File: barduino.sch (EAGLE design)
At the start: 28 parts, among them Q2 16MHz

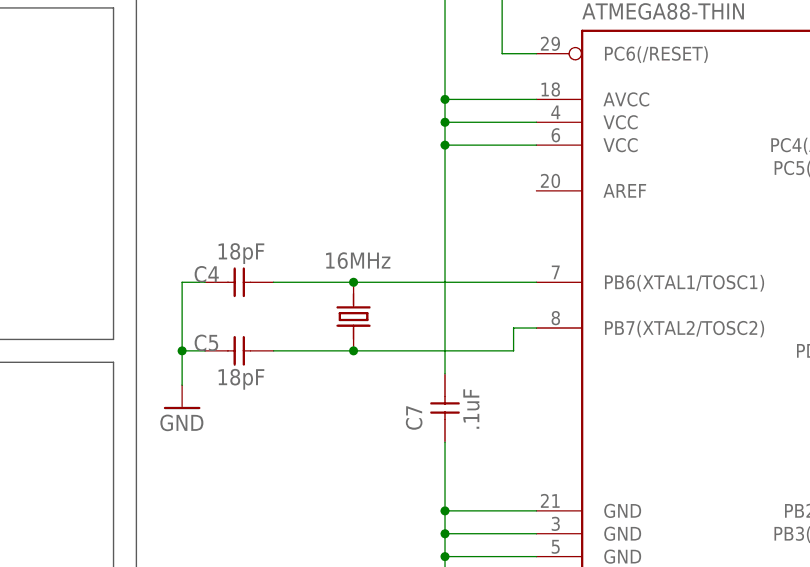
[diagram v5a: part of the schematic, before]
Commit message: replace crystal with new footprint part
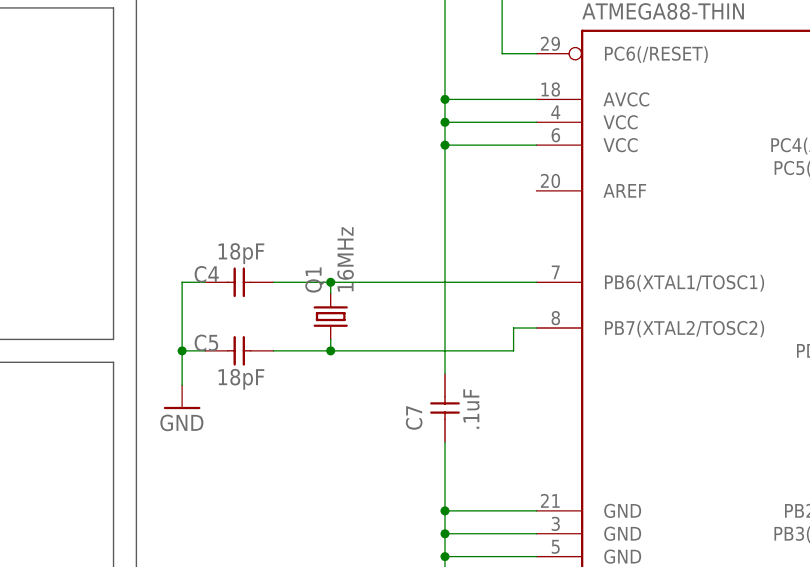
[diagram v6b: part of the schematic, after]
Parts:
- removed Q2: 16MHz, ng:CRYSTALCS10
- added Q1: 16MHz, crystal:CRYSTALHC49UP
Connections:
- net PB6: now also Q1.2; no longer Q2.2
- net PB7: now also Q1.1; no longer Q2.1
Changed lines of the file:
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@@
 <part name="P+3" library="supply1" deviceset="VCC" device=""/>
 <part name="GND4" library="supply1" deviceset="GND" device=""/>
-<part name="Q2" library="ng" deviceset="CRYSTAL" device="CS10" value="16MHz"/>
 <part name="C4" library="ng" deviceset="UNPOLARIZED_CAPACITOR" device="1206" value="18pF"/>
 <part name="C5" library="ng" deviceset="UNPOLARIZED_CAPACITOR" device="1206" value="18pF"/>
@@
 <part name="U$5" library="4-Digit-Clock" deviceset="MICRO-USB-PWR" device=""/>
 <part name="R13" library="resistor" library_urn="urn:adsk.eagle:library:348" deviceset="R-US_" device="R1206" package3d_urn="urn:adsk.eagle:package:26062/1"/>
+<part name="Q1" library="crystal" library_urn="urn:adsk.eagle:library:204" deviceset="CRYSTAL" device="HC49UP" package3d_urn="urn:adsk.eagle:package:12078/1" value="16MHz"/>
 </parts>
 <sheets>
@@
 <instance part="P+3" gate="VCC" x="213.36" y="110.49"/>
 <instance part="GND4" gate="1" x="184.15" y="45.72"/>
-<instance part="Q2" gate="G$1" x="203.2" y="55.88" smashed="yes" rot="R90">
-<attribute name="VALUE" x="199.898" y="61.214" size="1.778" layer="96"/>
-</instance>
 <instance part="C4" gate="1" x="191.77" y="59.69" smashed="yes">
 <attribute name="NAME" x="185.42" y="59.69" size="1.778" layer="95"/>
@@
 <instance part="U$5" gate="G$1" x="15.24" y="92.71" rot="MR0"/>
 <instance part="R13" gate="G$1" x="26.67" y="97.79" rot="R180"/>
+<instance part="Q1" gate="G$1" x="200.66" y="55.88" rot="R90"/>
 </instances>
 <busses>
@@
 <net name="PB7" class="0">
 <segment>
-<wire x1="203.2" y1="52.07" x2="194.31" y2="52.07" width="0.1524" layer="91"/>
-<pinref part="Q2" gate="G$1" pin="1"/>
 <pinref part="C5" gate="1" pin="2"/>
 <pinref part="U$1" gate="G$1" pin="PB7(XTAL2/TOSC2)"/>
 <wire x1="223.52" y1="54.61" x2="220.98" y2="54.61" width="0.1524" layer="91"/>
 <wire x1="220.98" y1="54.61" x2="220.98" y2="52.07" width="0.1524" layer="91"/>
-<wire x1="220.98" y1="52.07" x2="203.2" y2="52.07" width="0.1524" layer="91"/>
-<junction x="203.2" y="52.07"/>
+<wire x1="220.98" y1="52.07" x2="200.66" y2="52.07" width="0.1524" layer="91"/>
+<pinref part="Q1" gate="G$1" pin="1"/>
+<wire x1="200.66" y1="52.07" x2="194.31" y2="52.07" width="0.1524" layer="91"/>
+<wire x1="200.66" y1="53.34" x2="200.66" y2="52.07" width="0.1524" layer="91"/>
+<junction x="200.66" y="52.07"/>
 </segment>
 </net>
@@
 <net name="PB6" class="0">
 <segment>
-<wire x1="194.31" y1="59.69" x2="203.2" y2="59.69" width="0.1524" layer="91"/>
-<pinref part="Q2" gate="G$1" pin="2"/>
 <pinref part="C4" gate="1" pin="2"/>
 <pinref part="U$1" gate="G$1" pin="PB6(XTAL1/TOSC1)"/>
-<wire x1="223.52" y1="59.69" x2="203.2" y2="59.69" width="0.1524" layer="91"/>
-<junction x="203.2" y="59.69"/>
-</segment>
-</net>
+<wire x1="223.52" y1="59.69" x2="200.66" y2="59.69" width="0.1524" layer="91"/>
+<pinref part="Q1" gate="G$1" pin="2"/>
+<wire x1="200.66" y1="59.69" x2="194.31" y2="59.69" width="0.1524" layer="91"/>
+<wire x1="200.66" y1="58.42" x2="200.66" y2="59.69" width="0.1524" layer="91"/>
+<junction x="200.66" y="59.69"/>
+</segment>
+</net>

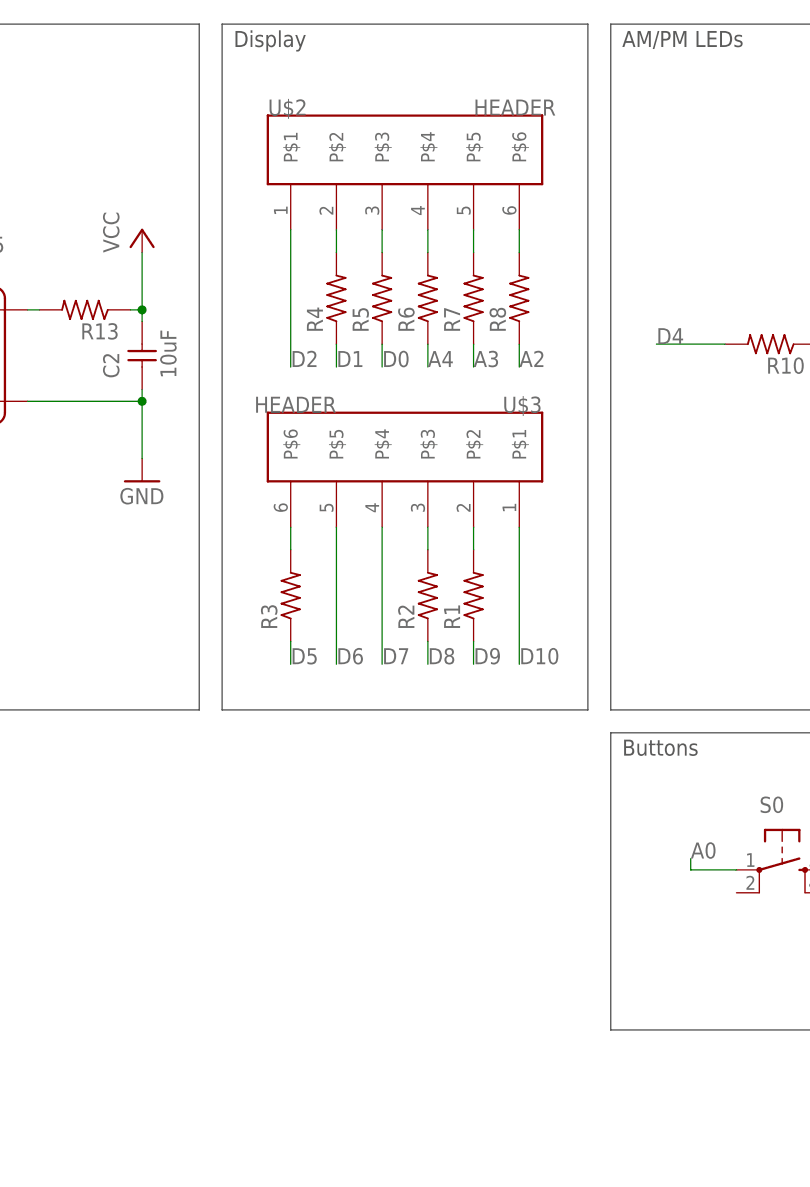
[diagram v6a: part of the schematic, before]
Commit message: add pull ups on display resistors
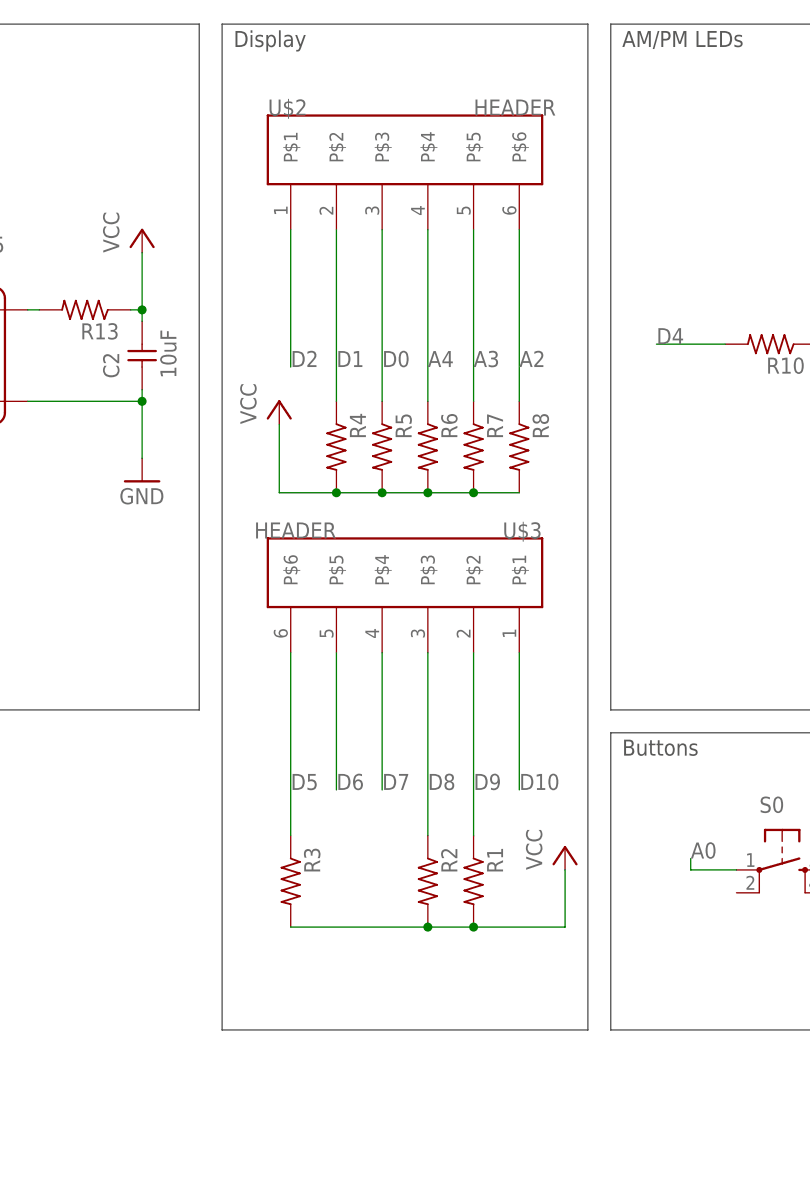
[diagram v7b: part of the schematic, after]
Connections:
- removed net N$10: R5.2, U$2.P$3
- removed net N$22: R4.2, U$2.P$2
- removed net N$23: R6.2, U$2.P$4
- removed net N$29: R2.2, U$3.P$3
- removed net N$33: R1.2, U$3.P$2
- removed net N$4: R3.2, U$3.P$6
- removed net N$8: R8.2, U$2.P$6
- removed net N$9: R7.2, U$2.P$5
- net A2: now also U$2.P$6
- net A3: now also U$2.P$5
- net A4: now also U$2.P$4
- net D0: now also U$2.P$3
- net D1: now also U$2.P$2
- net D5: now also U$3.P$6
- net D8: now also U$3.P$3
- net D9: now also U$3.P$2
- net VCC: now also R1.2, R2.2, R3.2, R4.2, R5.2, R6.2, R7.2, R8.2
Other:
- moved on the sheet: R1, R2, R3, R4, R5, R6, R7, R8, U$3

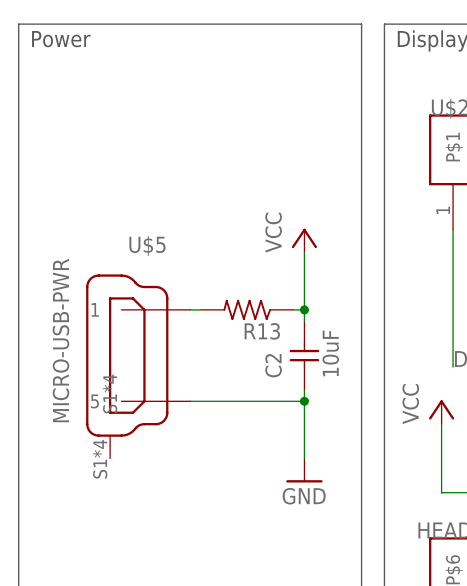
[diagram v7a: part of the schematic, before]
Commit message: change to new USB and buzzer footprint on schematic and layout
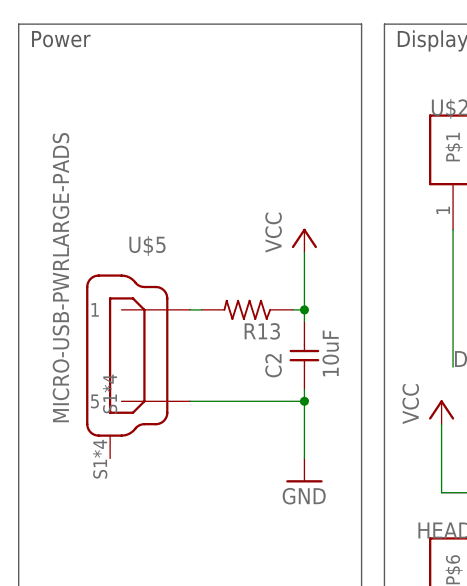
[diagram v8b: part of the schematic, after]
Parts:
- U$4: value BUZZER -> BUZZERLARGE-PADS; device 4-Digit-Clock:BUZZER -> 4-Digit-Clock:BUZZERLARGE-PADS
- U$5: value MICRO-USB-PWR -> MICRO-USB-PWRLARGE-PADS; device 4-Digit-Clock:MICRO-USB-PWR -> 4-Digit-Clock:MICRO-USB-PWRLARGE-PADS
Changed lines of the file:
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@@
 <grid distance="0.05" unitdist="inch" unit="inch" style="lines" multiple="1" display="no" altdistance="0.01" altunitdist="inch" altunit="inch"/>
 <layers>
-<layer number="1" name="Top" color="4" fill="1" visible="no" active="no"/>
-<layer number="2" name="Route2" color="1" fill="3" visible="no" active="no"/>
-<layer number="3" name="Route3" color="4" fill="3" visible="no" active="no"/>
-<layer number="4" name="Route4" color="1" fill="4" visible="no" active="no"/>
-<layer number="5" name="Route5" color="4" fill="4" visible="no" active="no"/>
-<layer number="6" name="Route6" color="1" fill="8" visible="no" active="no"/>
-<layer number="7" name="Route7" color="4" fill="8" visible="no" active="no"/>
-<layer number="8" name="Route8" color="1" fill="2" visible="no" active="no"/>
-<layer number="9" name="Route9" color="4" fill="2" visible="no" active="no"/>
-<layer number="10" name="Route10" color="1" fill="7" visible="no" active="no"/>
-<layer number="11" name="Route11" color="4" fill="7" visible="no" active="no"/>
-<layer number="12" name="Route12" color="1" fill="5" visible="no" active="no"/>
-<layer number="13" name="Route13" color="4" fill="5" visible="no" active="no"/>
-<layer number="14" name="Route14" color="1" fill="6" visible="no" active="no"/>
-<layer number="15" name="Route15" color="4" fill="6" visible="no" active="no"/>
-<layer number="16" name="Bottom" color="1" fill="1" visible="no" active="no"/>
-<layer number="17" name="Pads" color="2" fill="1" visible="no" active="no"/>
-<layer number="18" name="Vias" color="2" fill="1" visible="no" active="no"/>
-<layer number="19" name="Unrouted" color="6" fill="1" visible="no" active="no"/>
-<layer number="20" name="Dimension" color="15" fill="1" visible="no" active="no"/>
-<layer number="21" name="tPlace" color="7" fill="1" visible="no" active="no"/>
-<layer number="22" name="bPlace" color="7" fill="1" visible="no" active="no"/>
-<layer number="23" name="tOrigins" color="15" fill="1" visible="no" active="no"/>
-<layer number="24" name="bOrigins" color="15" fill="1" visible="no" active="no"/>
-<layer number="25" name="tNames" color="7" fill="1" visible="no" active="no"/>
-<layer number="26" name="bNames" color="7" fill="1" visible="no" active="no"/>
-<layer number="27" name="tValues" color="7" fill="1" visible="no" active="no"/>
-<layer number="28" name="bValues" color="7" fill="1" visible="no" active="no"/>
+<layer number="1" name="Top" color="12" fill="1" visible="yes" active="no"/>
+<layer number="2" name="Route2" color="1" fill="3" visible="yes" active="no"/>
+<layer number="3" name="Route3" color="4" fill="3" visible="yes" active="no"/>
+<layer number="4" name="Route4" color="1" fill="4" visible="yes" active="no"/>
+<layer number="5" name="Route5" color="4" fill="4" visible="yes" active="no"/>
+<layer number="6" name="Route6" color="1" fill="8" visible="yes" active="no"/>
+<layer number="7" name="Route7" color="4" fill="8" visible="yes" active="no"/>
+<layer number="8" name="Route8" color="1" fill="2" visible="yes" active="no"/>
+<layer number="9" name="Route9" color="4" fill="2" visible="yes" active="no"/>
+<layer number="10" name="Route10" color="1" fill="7" visible="yes" active="no"/>
+<layer number="11" name="Route11" color="4" fill="7" visible="yes" active="no"/>
+<layer number="12" name="Route12" color="1" fill="5" visible="yes" active="no"/>
+<layer number="13" name="Route13" color="4" fill="5" visible="yes" active="no"/>
+<layer number="14" name="Route14" color="1" fill="6" visible="yes" active="no"/>
+<layer number="15" name="Route15" color="4" fill="6" visible="yes" active="no"/>
+<layer number="16" name="Bottom" color="1" fill="1" visible="yes" active="no"/>
+<layer number="17" name="Pads" color="2" fill="1" visible="yes" active="no"/>
+<layer number="18" name="Vias" color="2" fill="1" visible="yes" active="no"/>
+<layer number="19" name="Unrouted" color="6" fill="1" visible="yes" active="no"/>
+<layer number="20" name="Dimension" color="15" fill="1" visible="yes" active="no"/>
+<layer number="21" name="tPlace" color="7" fill="1" visible="yes" active="no"/>
+<layer number="22" name="bPlace" color="7" fill="1" visible="yes" active="no"/>
+<layer number="23" name="tOrigins" color="15" fill="1" visible="yes" active="no"/>
+<layer number="24" name="bOrigins" color="15" fill="1" visible="yes" active="no"/>
+<layer number="25" name="tNames" color="7" fill="1" visible="yes" active="no"/>
+<layer number="26" name="bNames" color="7" fill="1" visible="yes" active="no"/>
+<layer number="27" name="tValues" color="7" fill="1" visible="yes" active="no"/>
+<layer number="28" name="bValues" color="7" fill="1" visible="yes" active="no"/>
 <layer number="29" name="tStop" color="7" fill="3" visible="no" active="no"/>
 <layer number="30" name="bStop" color="7" fill="6" visible="no" active="no"/>
@@
 <layer number="35" name="tGlue" color="7" fill="4" visible="no" active="no"/>
 <layer number="36" name="bGlue" color="7" fill="5" visible="no" active="no"/>
-<layer number="37" name="tTest" color="7" fill="1" visible="no" active="no"/>
-<layer number="38" name="bTest" color="7" fill="1" visible="no" active="no"/>
+<layer number="37" name="tTest" color="7" fill="1" visible="yes" active="no"/>
+<layer number="38" name="bTest" color="7" fill="1" visible="yes" active="no"/>
 <layer number="39" name="tKeepout" color="4" fill="11" visible="no" active="no"/>
 <layer number="40" name="bKeepout" color="1" fill="11" visible="no" active="no"/>
@@
 <layer number="44" name="Drills" color="7" fill="1" visible="no" active="no"/>
 <layer number="45" name="Holes" color="7" fill="1" visible="no" active="no"/>
-<layer number="46" name="Milling" color="3" fill="1" visible="no" active="no"/>
-<layer number="47" name="Measures" color="7" fill="1" visible="no" active="no"/>
-<layer number="48" name="Document" color="7" fill="1" visible="no" active="no"/>
-<layer number="49" name="Reference" color="7" fill="1" visible="no" active="no"/>
-<layer number="50" name="dxf" color="7" fill="1" visible="no" active="no"/>
-<layer number="51" name="tDocu" color="7" fill="1" visible="no" active="no"/>
-<layer number="52" name="bDocu" color="7" fill="1" visible="no" active="no"/>
-<layer number="53" name="tGND_GNDA" color="7" fill="9" visible="no" active="no"/>
-<layer number="54" name="bGND_GNDA" color="1" fill="9" visible="no" active="no"/>
-<layer number="56" name="wert" color="7" fill="1" visible="no" active="no"/>
-<layer number="57" name="tCAD" color="7" fill="1" visible="no" active="no"/>
-<layer number="59" name="tCarbon" color="7" fill="1" visible="no" active="no"/>
-<layer number="60" name="bCarbon" color="7" fill="1" visible="no" active="no"/>
+<layer number="46" name="Milling" color="3" fill="1" visible="yes" active="no"/>
+<layer number="47" name="Measures" color="7" fill="1" visible="yes" active="no"/>
+<layer number="48" name="Document" color="7" fill="1" visible="yes" active="no"/>
+<layer number="49" name="Reference" color="7" fill="1" visible="yes" active="no"/>
+<layer number="50" name="dxf" color="7" fill="1" visible="yes" active="no"/>
+<layer number="51" name="tDocu" color="7" fill="1" visible="yes" active="no"/>
+<layer number="52" name="bDocu" color="7" fill="1" visible="yes" active="no"/>
+<layer number="53" name="tGND_GNDA" color="7" fill="9" visible="yes" active="no"/>
+<layer number="54" name="bGND_GNDA" color="1" fill="9" visible="yes" active="no"/>
+<layer number="56" name="wert" color="7" fill="1" visible="yes" active="no"/>
+<layer number="57" name="tCAD" color="7" fill="1" visible="yes" active="no"/>
+<layer number="59" name="tCarbon" color="7" fill="1" visible="yes" active="no"/>
+<layer number="60" name="bCarbon" color="7" fill="1" visible="yes" active="no"/>
 <layer number="90" name="Modules" color="5" fill="1" visible="yes" active="yes"/>
 <layer number="91" name="Nets" color="2" fill="1" visible="yes" active="yes"/>
@@
 <part name="GND7" library="supply1" library_urn="urn:adsk.eagle:library:371" deviceset="GND" device=""/>
 <part name="GND3" library="supply1" library_urn="urn:adsk.eagle:library:371" deviceset="GND" device=""/>
-<part name="U$4" library="4-Digit-Clock" deviceset="BUZZER" device=""/>
+<part name="U$4" library="4-Digit-Clock" deviceset="BUZZER" device="LARGE-PADS" value="BUZZERLARGE-PADS"/>
 <part name="R1" library="resistor" library_urn="urn:adsk.eagle:library:348" deviceset="R-US_" device="R1206" package3d_urn="urn:adsk.eagle:package:26062/1"/>
 <part name="R2" library="resistor" library_urn="urn:adsk.eagle:library:348" deviceset="R-US_" device="R1206" package3d_urn="urn:adsk.eagle:package:26062/1"/>
@@
 <part name="R11" library="resistor" library_urn="urn:adsk.eagle:library:348" deviceset="R-US_" device="R1206" package3d_urn="urn:adsk.eagle:package:26062/1"/>
 <part name="R10" library="resistor" library_urn="urn:adsk.eagle:library:348" deviceset="R-US_" device="R1206" package3d_urn="urn:adsk.eagle:package:26062/1"/>
-<part name="U$5" library="4-Digit-Clock" deviceset="MICRO-USB-PWR" device=""/>
+<part name="U$5" library="4-Digit-Clock" deviceset="MICRO-USB-PWR" device="LARGE-PADS" value="MICRO-USB-PWRLARGE-PADS"/>
 <part name="R13" library="resistor" library_urn="urn:adsk.eagle:library:348" deviceset="R-US_" device="R1206" package3d_urn="urn:adsk.eagle:package:26062/1"/>
 <part name="Q1" library="crystal" library_urn="urn:adsk.eagle:library:204" deviceset="CRYSTAL" device="HC49UP" package3d_urn="urn:adsk.eagle:package:12078/1" value="16MHz"/>
